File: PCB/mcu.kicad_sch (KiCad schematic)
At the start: 13 parts, among them SW1 RST, SW2 BOOT, U1 STM32L432KCUx, Y2 32kHz

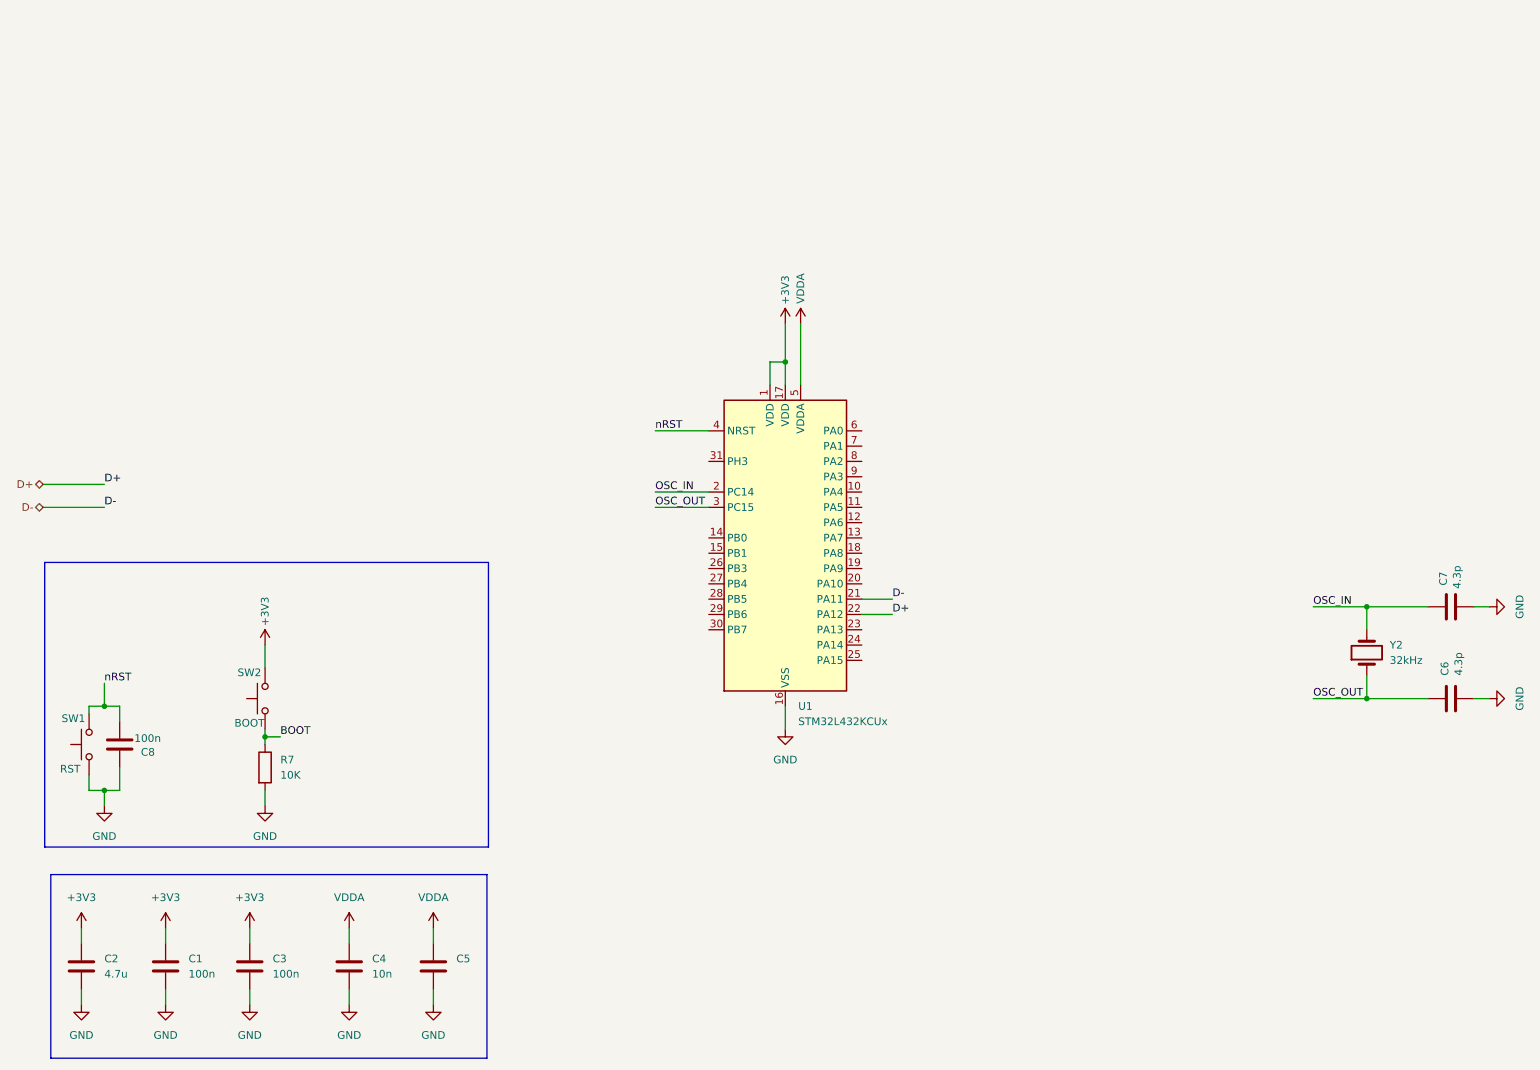
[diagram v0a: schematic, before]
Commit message: RFID sch added
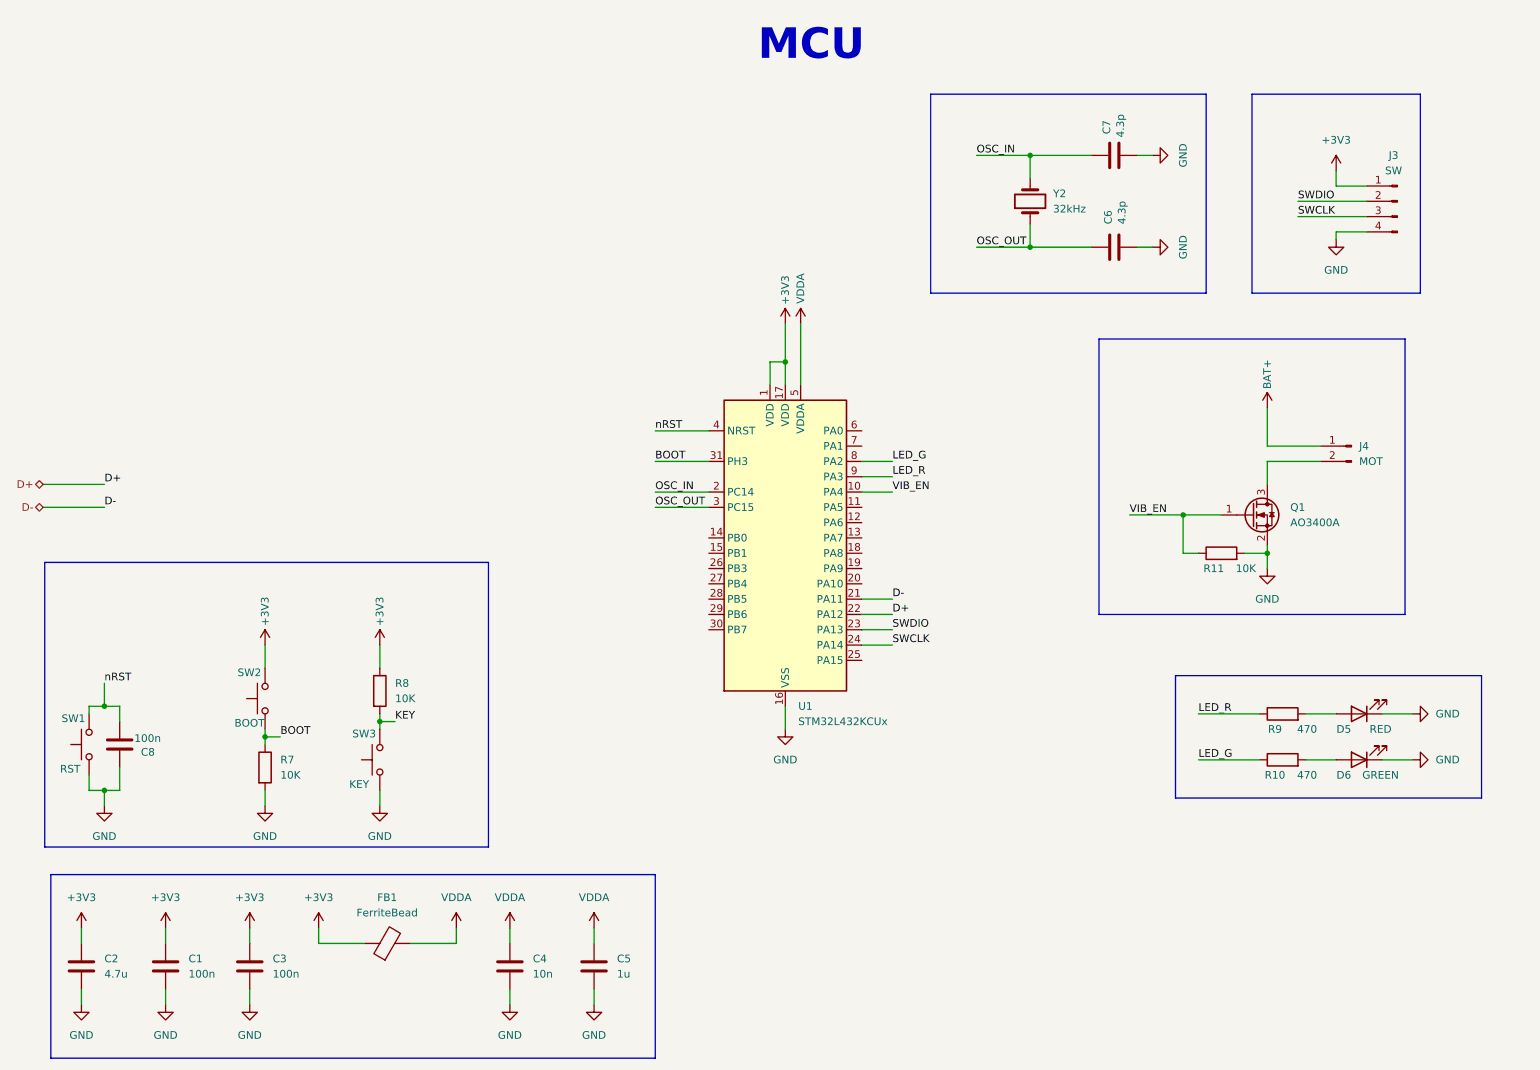
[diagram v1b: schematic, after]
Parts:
- added D5: RED, LED_SMD:LED_0805_2012Metric, symbol Device:LED
- added D6: GREEN, LED_SMD:LED_0805_2012Metric, symbol Device:LED
- added FB1: FerriteBead, Inductor_SMD:L_0402_1005Metric, symbol Device:FerriteBead
- added J3: SW, Connector_PinHeader_2.54mm:PinHeader_1x04_P2.54mm_Vertical, symbol Connector:Conn_01x04_Pin
- added J4: MOT, Connector_PinHeader_2.54mm:PinHeader_1x02_P2.54mm_Vertical, symbol Connector:Conn_01x02_Pin
- added Q1: AO3400A, Package_TO_SOT_SMD:SOT-23, symbol Transistor_FET:AO3400A
- added R10, R9: 470, Resistor_SMD:R_0805_2012Metric, symbol Device:R
- added R11, R8: 10K, Resistor_SMD:R_0805_2012Metric, symbol Device:R
- added SW3: KEY, Button_Switch_SMD:SW_Tactile_SPST_NO_Straight_CK_PTS636Sx25SMTRLFS, symbol Switch:SW_Push
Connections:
- net +3V3: now also FB1.1, J3.1 (Pin_1), R8.1
- net BOOT: now also U1.31 (PH3)
- net GND: now also D5.1 (K), D6.1 (K), J3.4 (Pin_4), Q1.2 (S), R11.2, SW3.1
- net VDDA: now also FB1.2
- net VIB_EN: now reaches U1.10 (PA4)
- net VIB_EN: now also Q1.1 (G), R11.1
- net SWDIO: now reaches U1.23 (PA13)
- net SWDIO: now also J3.2 (Pin_2)
- net SWCLK: now reaches U1.24 (PA14)
- net SWCLK: now also J3.3 (Pin_3)
- net LED_G: now reaches U1.8 (PA2)
- net LED_G: now also R10.1
- net LED_R: now reaches U1.9 (PA3)
- net LED_R: now also R9.1
- new net: D6.2 (A), R10.2
- new net: J4.2 (Pin_2), Q1.3 (D)
- new net: D5.2 (A), R9.2
- new net BAT+: J4.1 (Pin_1)
- new net KEY: R8.2, SW3.2
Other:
- note added: "MCU"
- moved on the sheet: C4, C5, C6, C7, Y2
